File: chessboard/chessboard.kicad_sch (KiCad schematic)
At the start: 6 parts, among them J1 Conn_01x08, U73 AMS1117-3.3

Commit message: a
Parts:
- C1: renamed from C50; value 100uF -> 22uF; footprint (none) -> Capacitor_SMD:C_0805_2012Metric_Pad1.18x1.45mm_HandSolder
- C2: renamed from C49; value 2.2uF -> 22uF; footprint (none) -> Capacitor_SMD:C_0805_2012Metric_Pad1.18x1.45mm_HandSolder
- J1: footprint (none) -> Connector_JST:JST_PH_B8B-PH-K_1x08_P2.00mm_Vertical
- JP1: renamed from JP33; footprint (none) -> TestPoint:TestPoint_Bridge_Pitch2.54mm_Drill1.0mm
- renumbered U73 to U1
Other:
- note added: "3.3V net capacitance 22uF (need) 64 * 100nF (sensors) + 8 * 2.2uF (multiplexers) = 7.2uF. Going to put 22uF near IC anyway."
- note removed: "3.3V capacitance 22uF (need) - 64 * 100nF (sensors) + 8 * 2.2uF (multiplexers) ought to be enough. Going to put one near IC anyway. Total = 26.2uF"

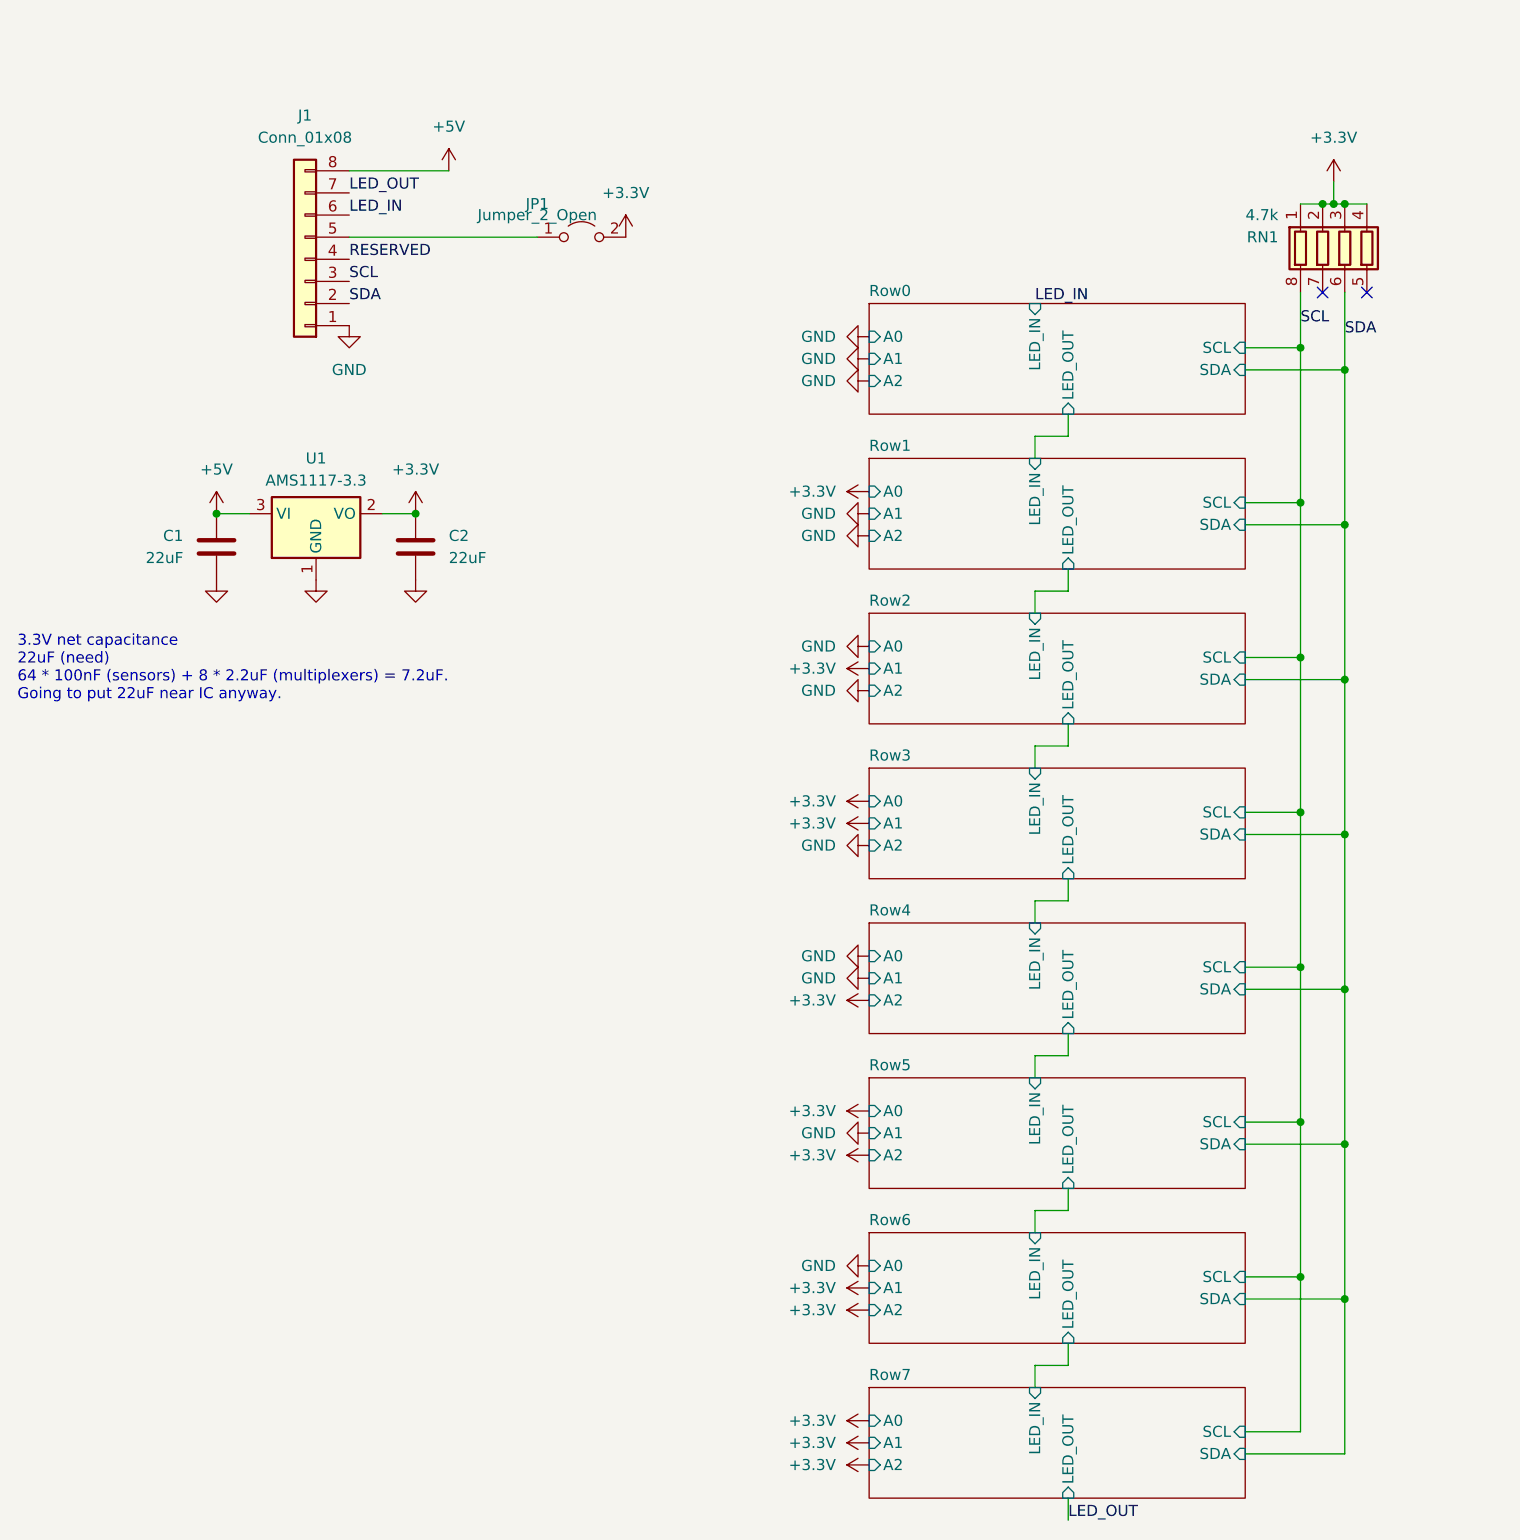
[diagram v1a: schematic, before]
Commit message: new single row board
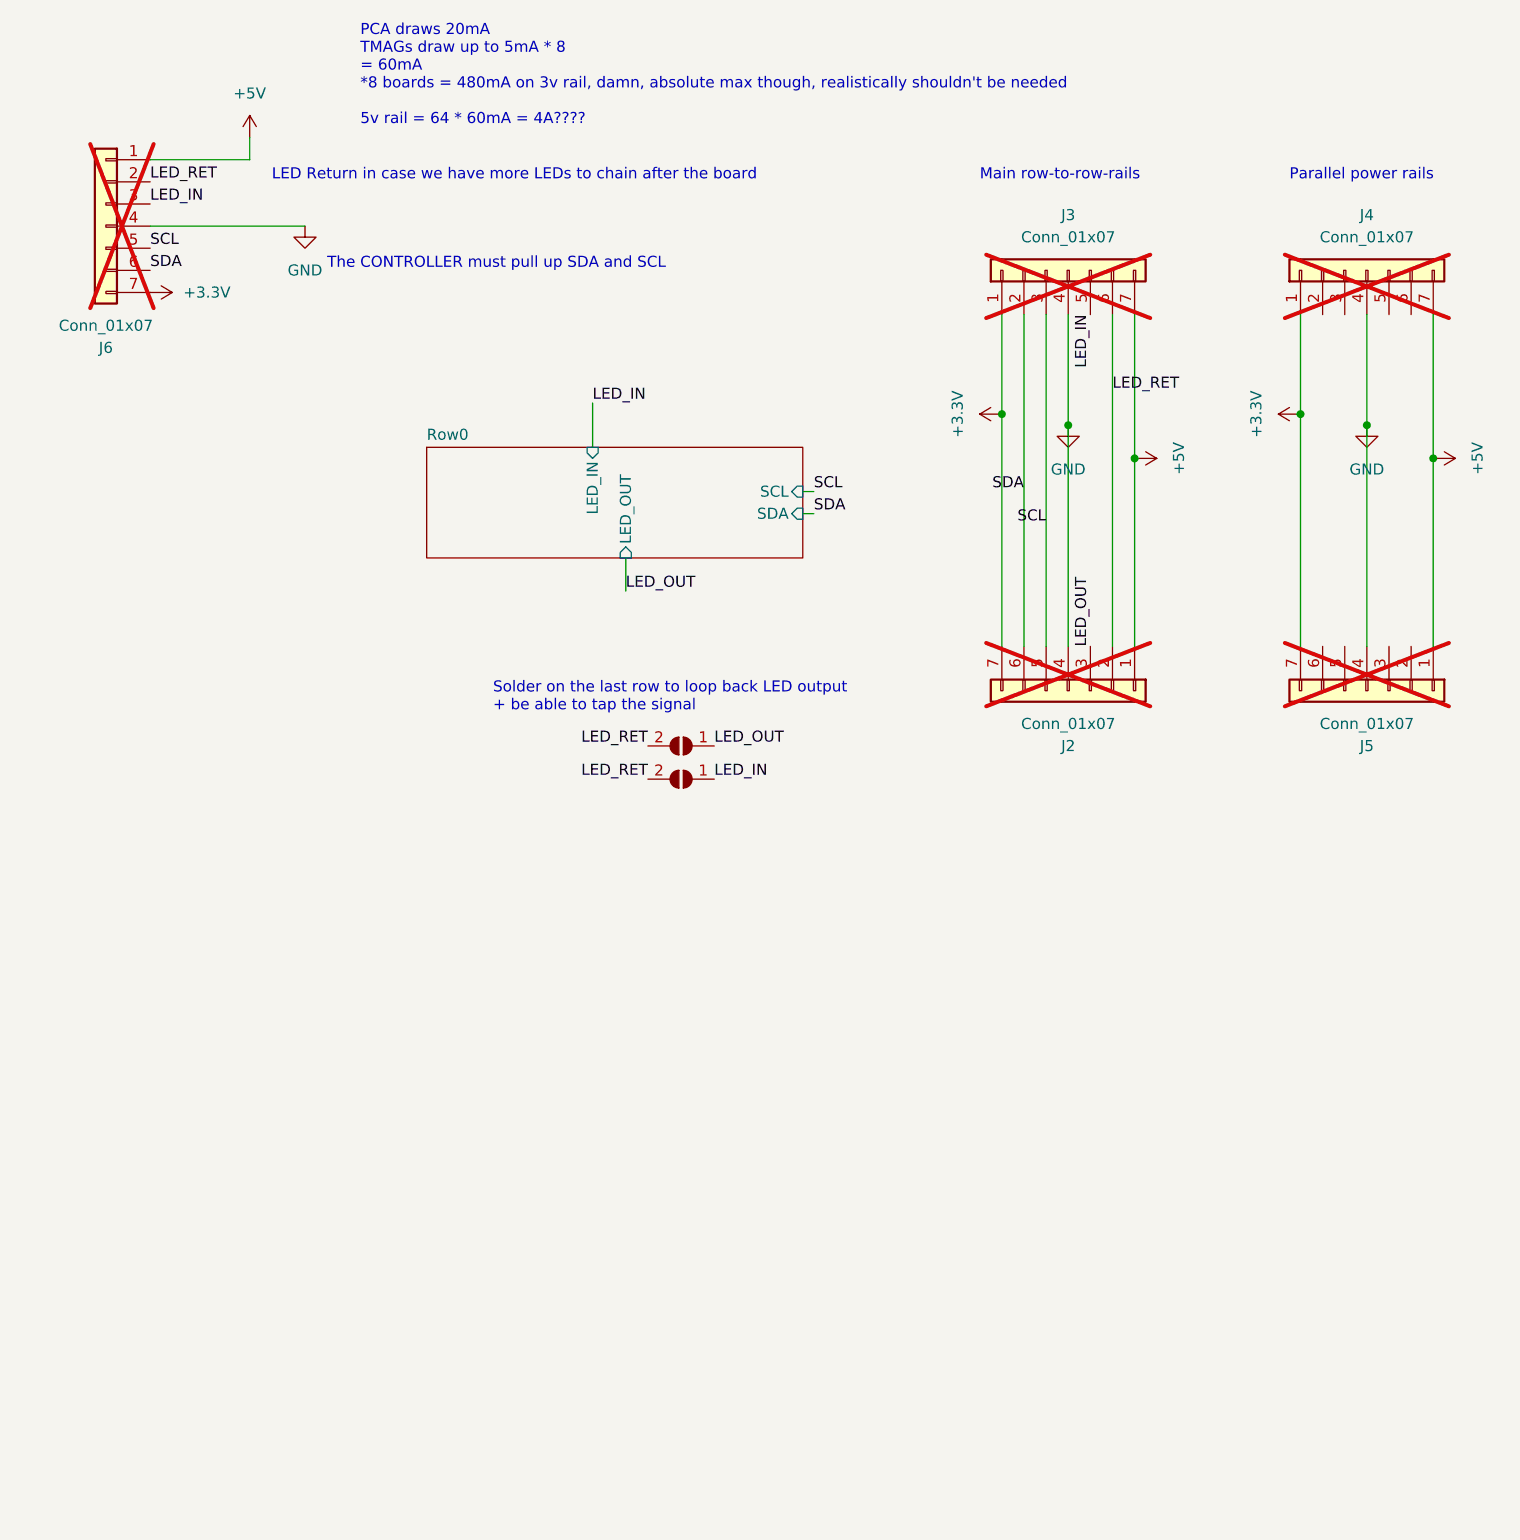
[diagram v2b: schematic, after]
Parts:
- removed C1, C2: 22uF, Capacitor_SMD:C_0805_2012Metric_Pad1.18x1.45mm_HandSolder, symbol Device:C
- removed J1: Conn_01x08, Connector_JST:JST_PH_B8B-PH-K_1x08_P2.00mm_Vertical, symbol Connector_Generic:Conn_01x08
- removed JP1: Jumper_2_Open, TestPoint:TestPoint_Bridge_Pitch2.54mm_Drill1.0mm, symbol Jumper:Jumper_2_Open
- removed RN1: 4.7k, Resistor_SMD:R_Array_Concave_4x0603, symbol Device:R_Pack04
- removed U1: AMS1117-3.3, Package_TO_SOT_SMD:SOT-223-3_TabPin2, symbol Regulator_Linear:AMS1117-3.3
- added J2, J3, J4, J5, J6: Conn_01x07, mylibrary:Custom PinSocket Edge Connector, symbol Connector_Generic:Conn_01x07
- added JP1, JP6: SolderJumper_2_Open, Resistor_SMD:R_0805_2012Metric_Pad1.20x1.40mm_HandSolder, symbol Jumper:SolderJumper_2_Open
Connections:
- net +3.3V: now also J2.7 (Pin_7), J3.1 (Pin_1), J4.1 (Pin_1), J5.7 (Pin_7), J6.7 (Pin_7)
- net +5V: now also J2.1 (Pin_1), J3.7 (Pin_7), J4.7 (Pin_7), J5.1 (Pin_1), J6.1 (Pin_1)
- net GND: now also J2.4 (Pin_4), J3.4 (Pin_4), J4.4 (Pin_4), J5.4 (Pin_4), J6.4 (Pin_4)
- net LED_IN: now also J3.5 (Pin_5), J6.3 (Pin_3), JP6.1 (A)
- net LED_OUT: now also J2.3 (Pin_3), JP1.1 (A)
- net SCL: now also J2.5 (Pin_5), J3.3 (Pin_3), J6.5 (Pin_5)
- net SDA: now also J2.6 (Pin_6), J3.2 (Pin_2), J6.6 (Pin_6)
- new net LED_RET: J2.2 (Pin_2), J3.6 (Pin_6), J6.2 (Pin_2), JP1.2 (B), JP6.2 (B)
- no-connect marks 2 -> 0
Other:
- removed sheet Row1
- removed sheet Row2
- removed sheet Row3
- removed sheet Row4
- removed sheet Row5
- removed sheet Row6
- removed sheet Row7
- sheet Row0 ports: added none; removed A0, A1, A2
- note added: "LED Return in case we have more LEDs to chain after the board"
- note added: "Main row-to-row-rails"
- note added: "PCA draws 20mA TMAGs draw up to 5mA * 8 = 60mA *8 boards = 480mA on 3v rail, damn, absolute max though, realistically shouldn't be needed 5v rail = 64 * 60mA = 4A????"
- note added: "Parallel power rails"
- note added: "Solder on the last row to loop back LED output + be able to tap the signal"
- note added: "The CONTROLLER must pull up SDA and SCL"
- note removed: "3.3V net capacitance 22uF (need) 64 * 100nF (sensors) + 8 * 2.2uF (multiplexers) = 7.2uF. Going to put 22uF near IC anyway."

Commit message: make it pretty
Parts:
- added H1, H2, H3: MountingHole_Pad, MountingHole:MountingHole_3.2mm_M3_ISO14580_Pad, symbol Mechanical:MountingHole_Pad
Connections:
- net GND: now also H1.1, H2.1, H3.1
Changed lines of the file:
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@@
     (effects (font (size 1.27 1.27)) (justify right bottom))
+  )
+  (symbol (lib_id "power:GND") (at 26.67 83.82 0) (unit 1)
+    (in_bom yes) (on_board yes) (dnp no) (fields_autoplaced)
+    (property "Reference" "#PWR041" (at 26.67 90.17 0)
+      (effects (font (size 1.27 1.27)) hide)
+    )
+    (property "Value" "GND" (at 26.67 88.9 0)
+      (effects (font (size 1.27 1.27)) hide)
+    )
+    (property "Footprint" "" (at 26.67 83.82 0)
+      (effects (font (size 1.27 1.27)) hide)
+    )
+    (property "Datasheet" "" (at 26.67 83.82 0)
+      (effects (font (size 1.27 1.27)) hide)
+    )
+    (pin "1")
+    (instances
+      (project "chessboard"
+        (path "/178674ef-da23-4447-9d4b-ea3429461404"
+          (reference "#PWR041") (unit 1)
+        )
+      )
+    )
   )
   (symbol (lib_id "power:GND") (at 54.61 38.1 0) (unit 1)
@@
     )
   )
+  (symbol (lib_id "Mechanical:MountingHole_Pad") (at 26.67 63.5 0) (unit 1)
+    (in_bom yes) (on_board yes) (dnp no) (fields_autoplaced)
+    (property "Reference" "H1" (at 29.21 60.96 0)
+      (effects (font (size 1.27 1.27)) (justify left))
+    )
+    (property "Value" "MountingHole_Pad" (at 29.21 63.5 0)
+      (effects (font (size 1.27 1.27)) (justify left))
+    )
+    (property "Footprint" "MountingHole:MountingHole_3.2mm_M3_ISO14580_Pad" (at 26.67 63.5 0)
+      (effects (font (size 1.27 1.27)) hide)
+    )
+    (property "Datasheet" "~" (at 26.67 63.5 0)
+      (effects (font (size 1.27 1.27)) hide)
+    )
+    (pin "1")
+    (instances
+      (project "chessboard"
+        (path "/178674ef-da23-4447-9d4b-ea3429461404"
+          (reference "H1") (unit 1)
+        )
+      )
+    )
+  )
   (symbol (lib_id "Connector_Generic:Conn_01x07") (at 31.75 38.1 0) (mirror y) (unit 1)
     (in_bom no) (on_board yes) (dnp yes)
@@
     )
   )
+  (symbol (lib_id "Mechanical:MountingHole_Pad") (at 26.67 81.28 0) (unit 1)
+    (in_bom yes) (on_board yes) (dnp no) (fields_autoplaced)
+    (property "Reference" "H3" (at 29.21 78.74 0)
+      (effects (font (size 1.27 1.27)) (justify left))
+    )
+    (property "Value" "MountingHole_Pad" (at 29.21 81.28 0)
+      (effects (font (size 1.27 1.27)) (justify left))
+    )
+    (property "Footprint" "MountingHole:MountingHole_3.2mm_M3_ISO14580_Pad" (at 26.67 81.28 0)
+      (effects (font (size 1.27 1.27)) hide)
+    )
+    (property "Datasheet" "~" (at 26.67 81.28 0)
+      (effects (font (size 1.27 1.27)) hide)
+    )
+    (pin "1")
+    (instances
+      (project "chessboard"
+        (path "/178674ef-da23-4447-9d4b-ea3429461404"
+          (reference "H3") (unit 1)
+        )
+      )
+    )
+  )
+  (symbol (lib_id "power:GND") (at 26.67 66.04 0) (unit 1)
+    (in_bom yes) (on_board yes) (dnp no) (fields_autoplaced)
+    (property "Reference" "#PWR039" (at 26.67 72.39 0)
+      (effects (font (size 1.27 1.27)) hide)
+    )
+    (property "Value" "GND" (at 26.67 71.12 0)
+      (effects (font (size 1.27 1.27)) hide)
+    )
+    (property "Footprint" "" (at 26.67 66.04 0)
+      (effects (font (size 1.27 1.27)) hide)
+    )
+    (property "Datasheet" "" (at 26.67 66.04 0)
+      (effects (font (size 1.27 1.27)) hide)
+    )
+    (pin "1")
+    (instances
+      (project "chessboard"
+        (path "/178674ef-da23-4447-9d4b-ea3429461404"
+          (reference "#PWR039") (unit 1)
+        )
+      )
+    )
+  )
+  (symbol (lib_id "Mechanical:MountingHole_Pad") (at 26.67 72.39 0) (unit 1)
+    (in_bom yes) (on_board yes) (dnp no) (fields_autoplaced)
+    (property "Reference" "H2" (at 29.21 69.85 0)
+      (effects (font (size 1.27 1.27)) (justify left))
+    )
+    (property "Value" "MountingHole_Pad" (at 29.21 72.39 0)
+      (effects (font (size 1.27 1.27)) (justify left))
+    )
+    (property "Footprint" "MountingHole:MountingHole_3.2mm_M3_ISO14580_Pad" (at 26.67 72.39 0)
+      (effects (font (size 1.27 1.27)) hide)
+    )
+    (property "Datasheet" "~" (at 26.67 72.39 0)
+      (effects (font (size 1.27 1.27)) hide)
+    )
+    (pin "1")
+    (instances
+      (project "chessboard"
+        (path "/178674ef-da23-4447-9d4b-ea3429461404"
+          (reference "H2") (unit 1)
+        )
+      )
+    )
+  )
   (symbol (lib_id "power:GND") (at 142.24 60.96 0) (mirror y) (unit 1)
     (in_bom yes) (on_board yes) (dnp no) (fields_autoplaced)
@@
         )
       )
+    )
+  )
+  (symbol (lib_id "power:GND") (at 26.67 74.93 0) (unit 1)
+    (in_bom yes) (on_board yes) (dnp no) (fields_autoplaced)
+    (property "Reference" "#PWR040" (at 26.67 81.28 0)
+      (effects (font (size 1.27 1.27)) hide)
+    )
+    (property "Value" "GND" (at 26.67 80.01 0)
+      (effects (font (size 1.27 1.27)) hide)
+    )
+    (property "Footprint" "" (at 26.67 74.93 0)
+      (effects (font (size 1.27 1.27)) hide)
+    )
+    (property "Datasheet" "" (at 26.67 74.93 0)
+      (effects (font (size 1.27 1.27)) hide)
+    )
+    (pin "1")
+    (instances
+      (project "chessboard"
+        (path "/178674ef-da23-4447-9d4b-ea3429461404"
+          (reference "#PWR040") (unit 1)
+        )
+      )
